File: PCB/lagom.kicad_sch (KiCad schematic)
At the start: 154 parts

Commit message: Matrix almost done
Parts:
- added D? (x2): D_Small, Keebio-Parts:Diode, symbol Device:D_Small
- added SW?: KEYSW, Button_Switch_Keyboard:SW_Cherry_MX_7u_PCB, symbol keyboard_parts:KEYSW
- added SW? (x2): KEYSW, Button_Switch_Keyboard:SW_Cherry_MX_1.00u_PCB, symbol keyboard_parts:KEYSW
- added SW?: KEYSW, Button_Switch_Keyboard:SW_Cherry_MX_1.50u_PCB, symbol keyboard_parts:KEYSW
- added SW? (x2): KEYSW, Button_Switch_Keyboard:SW_Cherry_MX_1.25u_PCB, symbol keyboard_parts:KEYSW
- SW?: footprint Button_Switch_Keyboard:SW_Cherry_MX_1.25u_PCB -> Button_Switch_Keyboard:SW_Cherry_MX_1.50u_PCB
- SW? (x2): footprint Button_Switch_Keyboard:SW_Cherry_MX_1.00u_PCB -> Button_Switch_Keyboard:SW_Cherry_MX_1.25u_PCB
- SW?: footprint Button_Switch_Keyboard:SW_Cherry_MX_1.00u_PCB -> Button_Switch_Keyboard:SW_Cherry_MX_1.50u_PCB
- SW?: footprint Button_Switch_Keyboard:SW_Cherry_MX_1.25u_PCB -> Button_Switch_Keyboard:SW_Cherry_MX_1.00u_PCB
- SW?: footprint Button_Switch_Keyboard:SW_Cherry_MX_1.25u_PCB -> Button_Switch_Keyboard:SW_Cherry_MX_ISOEnter_PCB
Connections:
- net RotA: now also D?.2 (A); no longer D?.2 (A)
- net RotB: now also SW?.1, SW?.1, SW?.1, SW?.1; no longer SW?.1, SW?.1, SW?.1, SW?.1
- net RotC: now also D?.2 (A); no longer D?.2 (A)
- net RotD: now also SW?.1, SW?.1, SW?.1, SW?.1, SW?.1; no longer SW?.1, SW?.1, SW?.1, SW?.1
- net rowG: now also D?.1 (K), D?.1 (K); no longer U?.20 (A3/PF4)
- net at SW?.1, SW?.1, SW?.1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: now also SW?.1 (x2)
- net at SW?.1, SW?.1, SW?.1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: now also SW?.1
- net at D?.2 (A), SW?.2: now also SW?.2 (x3)
- net at SW?.1, SW?.1, SW?.1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: now also SW?.1
- net at D?.2 (A), SW?.2, SW?.2: now also SW?.2
- new net: SW?.1, SW?.1, SW?.1, SW?.1, SW?.1 (x2)
- new net: D?.2 (A), SW?.2 (x2)
- new net rowH: U?.20 (A3/PF4)
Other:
- moved on the sheet: SW?

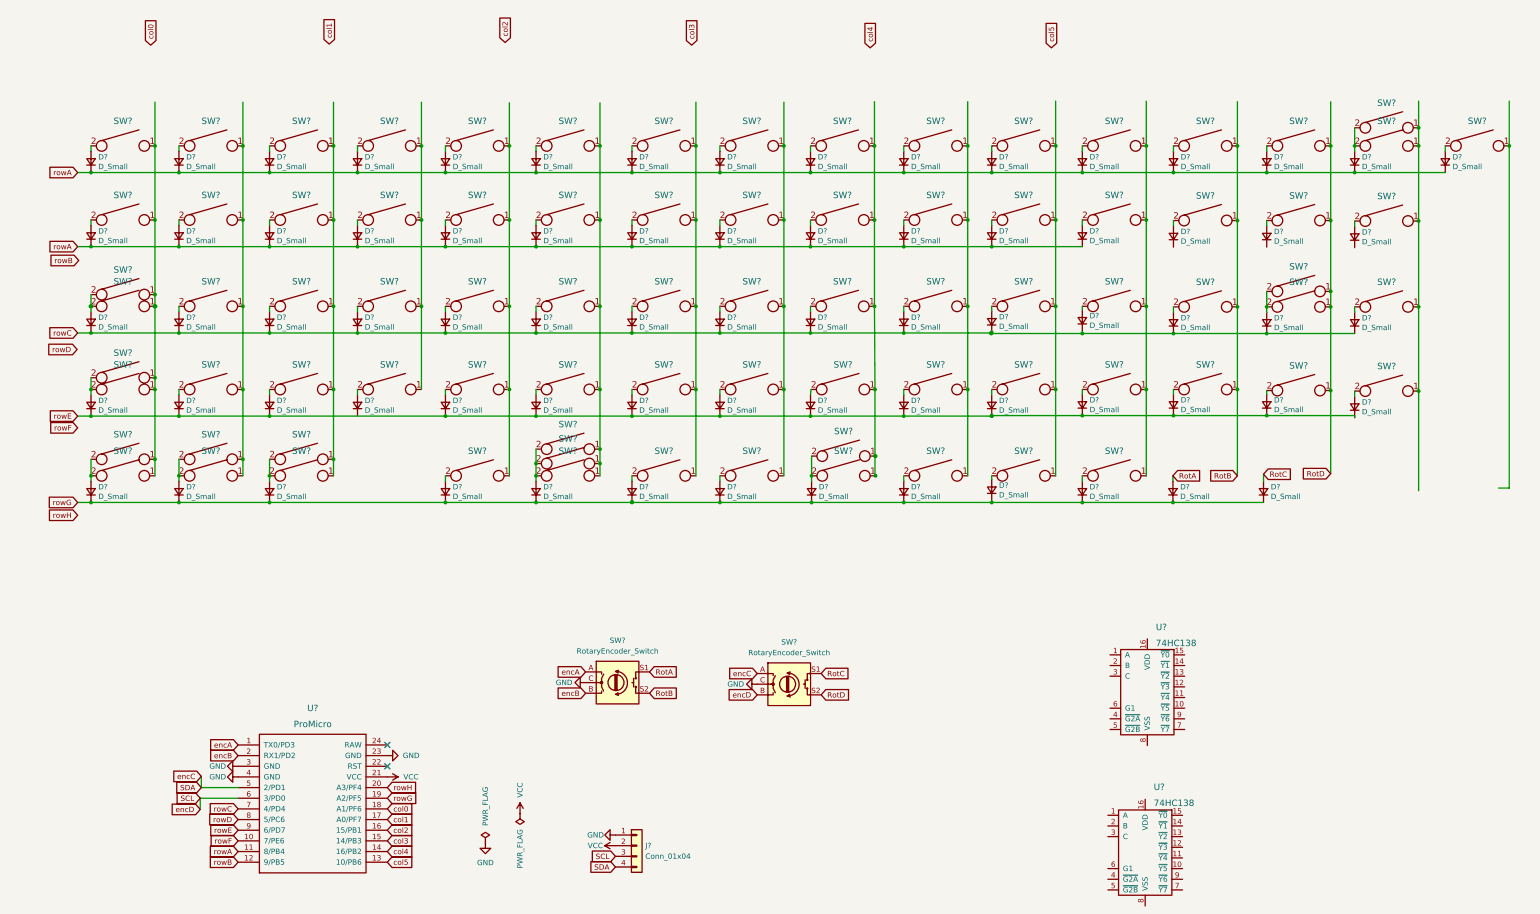
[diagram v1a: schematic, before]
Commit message: Matrix complete, wiring schematic
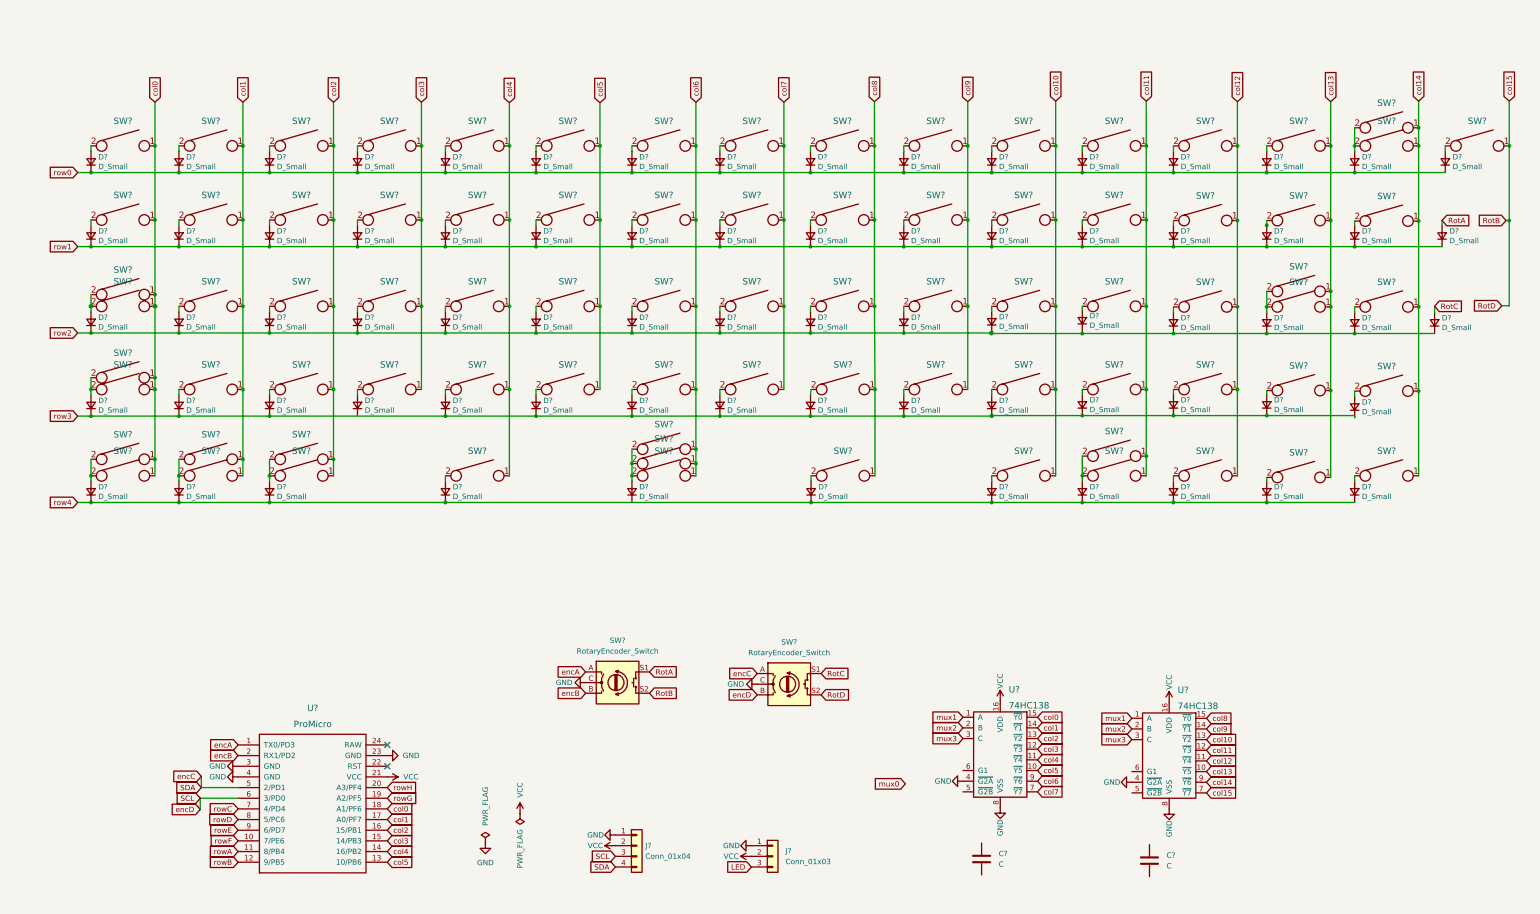
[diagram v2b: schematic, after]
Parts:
- added C? (x2): C, symbol Device:C
- added J?: Conn_01x03, symbol Connector_Generic:Conn_01x03
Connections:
- net GND: now also U?.4 (~{G2A}), U?.4 (~{G2A}), U?.8 (VSS), U?.8 (VSS), J?.1 (Pin_1)
- net RotB: now also SW?.1, SW?.S2, U?.7 (~{Y7}); no longer SW?.1, SW?.1, SW?.1, SW?.1
- net VCC: now also U?.16 (VDD), U?.16 (VDD), J?.2 (Pin_2)
- net col0: now also SW?.1, SW?.1, SW?.1, SW?.1, SW?.1, SW?.1, SW?.1, SW?.1, U?.15 (~{Y0})
- net col1: now also SW?.1, SW?.1, SW?.1, SW?.1, SW?.1, SW?.1, U?.14 (~{Y1})
- net col2: now also SW?.1, SW?.1, SW?.1, SW?.1, SW?.1, SW?.1, U?.13 (~{Y2})
- net col3: now also SW?.1, SW?.1, SW?.1, SW?.1, U?.12 (~{Y3})
- net col4: now also SW?.1, SW?.1, SW?.1, SW?.1, SW?.1, U?.11 (~{Y4})
- net col5: now also SW?.1, SW?.1, SW?.1, SW?.1, U?.10 (~{Y5})
- net rowA: no longer D?.1 (K), D?.1 (K), D?.1 (K), D?.1 (K), D?.1 (K), D?.1 (K), D?.1 (K), D?.1 (K), D?.1 (K), D?.1 (K), D?.1 (K), D?.1 (K), D?.1 (K), D?.1 (K), D?.1 (K), D?.1 (K), D?.1 (K), D?.1 (K), D?.1 (K), D?.1 (K), D?.1 (K), D?.1 (K), D?.1 (K), D?.1 (K)
- net rowC: no longer D?.1 (K), D?.1 (K), D?.1 (K), D?.1 (K), D?.1 (K), D?.1 (K), D?.1 (K), D?.1 (K), D?.1 (K), D?.1 (K), D?.1 (K), D?.1 (K), D?.1 (K), D?.1 (K), D?.1 (K)
- net rowE: no longer D?.1 (K), D?.1 (K), D?.1 (K), D?.1 (K), D?.1 (K), D?.1 (K), D?.1 (K), D?.1 (K), D?.1 (K), D?.1 (K), D?.1 (K), D?.1 (K), D?.1 (K), D?.1 (K)
- net rowG: no longer D?.1 (K), D?.1 (K), D?.1 (K), D?.1 (K), D?.1 (K), D?.1 (K), D?.1 (K), D?.1 (K), D?.1 (K), D?.1 (K), D?.1 (K), D?.1 (K), D?.1 (K)
- net col8: now reaches SW?.1, SW?.1, SW?.1, SW?.1
- net col8: now also SW?.1, U?.15 (~{Y0}); no longer SW?.1, SW?.1
- net col10: now reaches SW?.1, SW?.1, SW?.1, SW?.1
- net col10: now also SW?.1, U?.13 (~{Y2}); no longer SW?.1
- net col9: now reaches SW?.1, SW?.1, SW?.1, SW?.1
- net col9: now also U?.14 (~{Y1}); no longer SW?.1
- net col14: now reaches SW?.1, SW?.1, SW?.1, SW?.1, SW?.1
- net col14: now also SW?.1, U?.9 (~{Y6})
- net row1: now reaches D?.1 (K)
- net row1: now also D?.1 (K), D?.1 (K), D?.1 (K), D?.1 (K), D?.1 (K), D?.1 (K), D?.1 (K), D?.1 (K), D?.1 (K), D?.1 (K), D?.1 (K), D?.1 (K), D?.1 (K), D?.1 (K), D?.1 (K)
- net col7: now reaches SW?.1, SW?.1, SW?.1, SW?.1
- net col7: now also U?.7 (~{Y7}); no longer SW?.1
- net col6: now reaches SW?.1, SW?.1, SW?.1, SW?.1
- net col6: now also SW?.1, SW?.1, SW?.1, U?.9 (~{Y6}); no longer SW?.1
- net col11: now reaches SW?.1, SW?.1, SW?.1, SW?.1
- net col11: now also SW?.1, SW?.1, U?.12 (~{Y3}); no longer SW?.1
- net mux1: now reaches U?.1 (A)
- net mux1: now also U?.1 (A)
- net mux2: now reaches U?.2 (B)
- net mux2: now also U?.2 (B)
- net mux3: now reaches U?.3 (C)
- net mux3: now also U?.3 (C)
- net col13: now reaches U?.10 (~{Y5})
- net col13: now also SW?.1, SW?.1, SW?.1, SW?.1, SW?.1, SW?.1
- net col12: now reaches U?.11 (~{Y4})
- net col12: now also SW?.1, SW?.1, SW?.1, SW?.1, SW?.1
- removed net RotD: SW?.1, SW?.1, SW?.1, SW?.1, SW?.1, SW?.S2
- new net LED: J?.3 (Pin_3)
- new net row0: D?.1 (K), D?.1 (K), D?.1 (K), D?.1 (K), D?.1 (K), D?.1 (K), D?.1 (K), D?.1 (K), D?.1 (K), D?.1 (K), D?.1 (K), D?.1 (K)
- new net row2: D?.1 (K), D?.1 (K), D?.1 (K), D?.1 (K), D?.1 (K), D?.1 (K), D?.1 (K), D?.1 (K), D?.1 (K), D?.1 (K), D?.1 (K), D?.1 (K), D?.1 (K), D?.1 (K), D?.1 (K), D?.1 (K)
- new net row3: D?.1 (K), D?.1 (K), D?.1 (K), D?.1 (K), D?.1 (K), D?.1 (K), D?.1 (K), D?.1 (K), D?.1 (K), D?.1 (K), D?.1 (K), D?.1 (K), D?.1 (K), D?.1 (K)
- new net row4: D?.1 (K), D?.1 (K), D?.1 (K), D?.1 (K), D?.1 (K), D?.1 (K), D?.1 (K), D?.1 (K), D?.1 (K), D?.1 (K)
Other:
- moved on the sheet: D?, SW?, U?

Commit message: Schematic complete
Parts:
- C1, C2: renamed from C?; value C -> 0.1uF
- D1: renamed from D?; footprint Keebio-Parts:Diode -> Diode_THT:D_DO-35_SOD27_P7.62mm_Horizontal
- gave numbers to parts that had none: 162
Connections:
- net rowA is gone; now on net row3: U1.11 (8/PB4)
- net rowB is gone; now on net row4: U1.12 (9/PB5)
- net rowC is gone; now on net LED: U1.7 (4/PD4)
- net rowD is gone; now on net row0: U1.8 (5/PC6)
- net rowE is gone; now on net row1: U1.9 (6/PD7)
- net rowF is gone; now on net row2: U1.10 (7/PE6)
- net rowG is gone; now on net encB: U1.19 (A2/PF5)
- net rowH is gone; now on net encA: U1.20 (A3/PF4)
- net GND: now also C1.2, C2.2, U3.5 (~{G2B})
- net SCL: no longer SW84.B
- net SDA: no longer SW84.A
- net VCC: now also C1.1, C2.1, U2.6 (G1)
- net col0: no longer U1.18 (A1/PF6)
- net col1: no longer U1.17 (A0/PF7)
- net col2: no longer U1.16 (15/PB1)
- net col3: no longer U1.15 (14/PB3)
- net col4: no longer U1.14 (16/PB2)
- net col5: no longer U1.13 (10/PB6)
- net encA: no longer U1.1 (TX0/PD3)
- net encB: no longer U1.2 (RX1/PD2)
- net mux0: now also U1.16 (15/PB1), U2.5 (~{G2B}), U3.6 (G1)
- net mux1: now also U1.15 (14/PB3)
- net mux2: now also U1.14 (16/PB2)
- net mux3: now also U1.13 (10/PB6)
- net row3: now also D55.1 (K)
- net row4: now also D68.1 (K)
- new net encC: SW84.A, U1.18 (A1/PF6)
- new net encD: SW84.B, U1.17 (A0/PF7)
- no-connect marks 2 -> 4
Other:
- moved on the sheet: C1, C2, U1, U3

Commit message: PCB layout done
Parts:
- C1, C2: footprint (none) -> Capacitor_THT:C_Disc_D4.7mm_W2.5mm_P5.00mm
- J2: footprint (none) -> Connector_PinSocket_2.54mm:PinSocket_1x03_P2.54mm_Vertical
- SW13, SW17, SW29: footprint Button_Switch_Keyboard:SW_Cherry_MX_1.50u_PCB -> Button_Switch_Keyboard:SW_Cherry_MX_1.00u_PCB
- U2, U3: footprint (none) -> Package_DIP:DIP-16_W7.62mm_Socket
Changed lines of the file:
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@@
       (effects (font (size 1.27 1.27)) (justify left))
     )
-    (property "Footprint" "" (id 2) (at 246.8372 199.898 0)
+    (property "Footprint" "Capacitor_THT:C_Disc_D4.7mm_W2.5mm_P5.00mm" (id 2) (at 246.8372 199.898 0)
       (effects (font (size 1.27 1.27)) hide)
     )
@@
   (symbol (lib_id "w_logic:74HC138") (at 269.621 195.58 0) (unit 1)
     (in_bom yes) (on_board yes) (fields_autoplaced)
-    (property "Reference" "U2" (id 0) (at 271.6404 180.086 0)
+    (property "Reference" "U2" (id 0) (at 271.6404 180.34 0)
       (effects (font (size 1.524 1.524)) (justify left))
     )
-    (property "Value" "74HC138" (id 1) (at 271.6404 183.896 0)
+    (property "Value" "74HC138" (id 1) (at 271.6404 184.15 0)
       (effects (font (size 1.524 1.524)) (justify left))
     )
-    (property "Footprint" "" (id 2) (at 269.621 195.58 0)
-      (effects (font (size 1.524 1.524)))
+    (property "Footprint" "Package_DIP:DIP-16_W7.62mm_Socket" (id 2) (at 269.621 195.58 0)
+      (effects (font (size 1.524 1.524)) hide)
     )
     (property "Datasheet" "/mnt/dati/documenti/Elettronica/DATA_SHEET/Elettronici/Integrati/Digitali/Registri/NXP_74HC138_74HCT138.pdf" (id 3) (at 271.6404 183.896 0)
@@
       (effects (font (size 1.524 1.524)) hide)
     )
-    (property "Footprint" "Button_Switch_Keyboard:SW_Cherry_MX_1.50u_PCB" (id 2) (at 383.286 50.546 0)
+    (property "Footprint" "Button_Switch_Keyboard:SW_Cherry_MX_1.00u_PCB" (id 2) (at 383.286 50.546 0)
       (effects (font (size 1.524 1.524)) hide)
     )
@@
       (effects (font (size 1.524 1.524)) hide)
     )
-    (property "Footprint" "Button_Switch_Keyboard:SW_Cherry_MX_1.50u_PCB" (id 2) (at 296.799 50.546 0)
+    (property "Footprint" "Button_Switch_Keyboard:SW_Cherry_MX_1.00u_PCB" (id 2) (at 296.799 50.546 0)
       (effects (font (size 1.524 1.524)) hide)
     )
@@
       (effects (font (size 1.27 1.27)) (justify left))
     )
-    (property "Footprint" "" (id 2) (at 215.392 219.837 0)
+    (property "Footprint" "Connector_PinSocket_2.54mm:PinSocket_1x03_P2.54mm_Vertical" (id 2) (at 215.392 219.837 0)
       (effects (font (size 1.27 1.27)) hide)
     )
@@
       (effects (font (size 1.27 1.27)) (justify left))
     )
-    (property "Footprint" "" (id 2) (at 305.5112 198.882 0)
+    (property "Footprint" "Capacitor_THT:C_Disc_D4.7mm_W2.5mm_P5.00mm" (id 2) (at 305.5112 198.882 0)
       (effects (font (size 1.27 1.27)) hide)
     )
@@
   (symbol (lib_id "w_logic:74HC138") (at 328.93 195.199 0) (unit 1)
     (in_bom yes) (on_board yes) (fields_autoplaced)
-    (property "Reference" "U3" (id 0) (at 330.9494 179.578 0)
+    (property "Reference" "U3" (id 0) (at 330.9494 179.07 0)
       (effects (font (size 1.524 1.524)) (justify left))
     )
-    (property "Value" "74HC138" (id 1) (at 330.9494 183.388 0)
+    (property "Value" "74HC138" (id 1) (at 330.9494 182.88 0)
       (effects (font (size 1.524 1.524)) (justify left))
     )
-    (property "Footprint" "" (id 2) (at 328.93 195.199 0)
-      (effects (font (size 1.524 1.524)))
+    (property "Footprint" "Package_DIP:DIP-16_W7.62mm_Socket" (id 2) (at 328.93 195.199 0)
+      (effects (font (size 1.524 1.524)) hide)
     )
     (property "Datasheet" "/mnt/dati/documenti/Elettronica/DATA_SHEET/Elettronici/Integrati/Digitali/Registri/NXP_74HC138_74HCT138.pdf" (id 3) (at 330.9494 183.515 0)
@@
       (effects (font (size 1.524 1.524)) hide)
     )
-    (property "Footprint" "Button_Switch_Keyboard:SW_Cherry_MX_1.50u_PCB" (id 2) (at 296.799 68.199 0)
+    (property "Footprint" "Button_Switch_Keyboard:SW_Cherry_MX_1.00u_PCB" (id 2) (at 296.799 68.199 0)
       (effects (font (size 1.524 1.524)) hide)
     )
@@
     )
     (path "/bc00cb6d-ff28-45b9-b930-be73b03fd96d"
-      (reference "C1") (unit 1) (value "0.1uF") (footprint "")
+      (reference "C1") (unit 1) (value "0.1uF") (footprint "Capacitor_THT:C_Disc_D4.7mm_W2.5mm_P5.00mm")
     )
     (path "/0fd8c6ab-3384-49aa-8e48-3f4df84bc20e"
-      (reference "C2") (unit 1) (value "0.1uF") (footprint "")
+      (reference "C2") (unit 1) (value "0.1uF") (footprint "Capacitor_THT:C_Disc_D4.7mm_W2.5mm_P5.00mm")
     )
     (path "/afa695ae-8ccf-42d3-9dcb-5e731da4e36c"
@@
     )
     (path "/afffe1fe-d14c-481c-bd58-ae7a8ca3d519"
-      (reference "J2") (unit 1) (value "Conn_01x03") (footprint "")
+      (reference "J2") (unit 1) (value "Conn_01x03") (footprint "Connector_PinSocket_2.54mm:PinSocket_1x03_P2.54mm_Vertical")
     )
     (path "/a5c5762f-a0e0-401e-8bc4-621198606bcb"
@@
     )
     (path "/9c21fdb3-4254-429a-8fa6-c29cf995b177"
-      (reference "SW13") (unit 1) (value "KEYSW") (footprint "Button_Switch_Keyboard:SW_Cherry_MX_1.50u_PCB")
+      (reference "SW13") (unit 1) (value "KEYSW") (footprint "Button_Switch_Keyboard:SW_Cherry_MX_1.00u_PCB")
     )
     (path "/fec9eaae-d6bc-4df4-9d8e-a08e2c64f06c"
@@
     )
     (path "/9808b20e-3499-4769-b8e9-46d57a37bd43"
-      (reference "SW17") (unit 1) (value "KEYSW") (footprint "Button_Switch_Keyboard:SW_Cherry_MX_1.50u_PCB")
+      (reference "SW17") (unit 1) (value "KEYSW") (footprint "Button_Switch_Keyboard:SW_Cherry_MX_1.00u_PCB")
     )
     (path "/05d4fb02-3c60-405c-9080-fb8446959d7e"
@@
     )
     (path "/e9fcf385-9380-4c87-8aca-dfe9bbcc7460"
-      (reference "SW29") (unit 1) (value "KEYSW") (footprint "Button_Switch_Keyboard:SW_Cherry_MX_1.50u_PCB")
+      (reference "SW29") (unit 1) (value "KEYSW") (footprint "Button_Switch_Keyboard:SW_Cherry_MX_1.00u_PCB")
     )
     (path "/71d08102-98f4-4a2d-8663-96fe9600f004"
@@
     )
     (path "/6894fe82-0ee5-4f27-a435-6dbd0d79b968"
-      (reference "U2") (unit 1) (value "74HC138") (footprint "")
+      (reference "U2") (unit 1) (value "74HC138") (footprint "Package_DIP:DIP-16_W7.62mm_Socket")
     )
     (path "/c92f95b2-2642-46df-8ce4-131bc603da4f"
-      (reference "U3") (unit 1) (value "74HC138") (footprint "")
+      (reference "U3") (unit 1) (value "74HC138") (footprint "Package_DIP:DIP-16_W7.62mm_Socket")
     )
   )

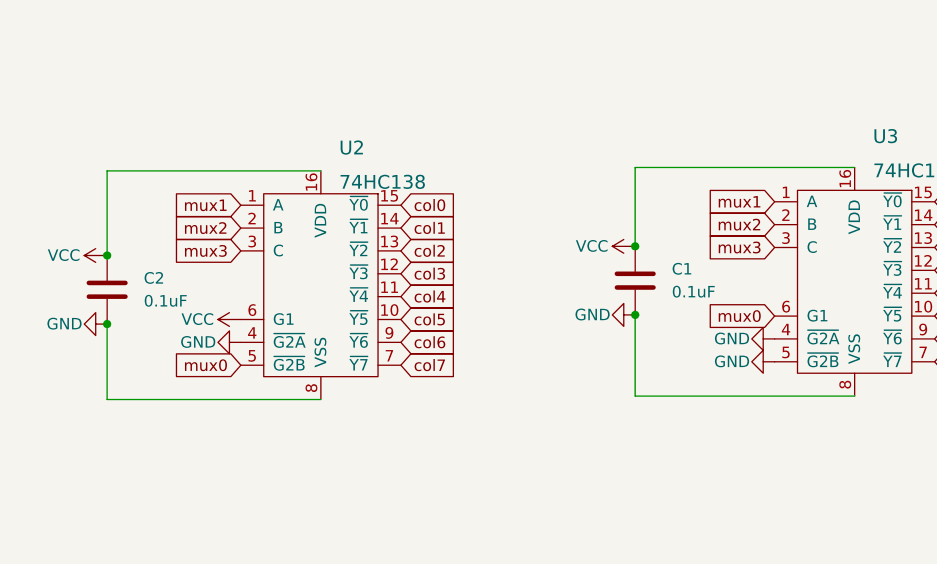
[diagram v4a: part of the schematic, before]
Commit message: demux pin change
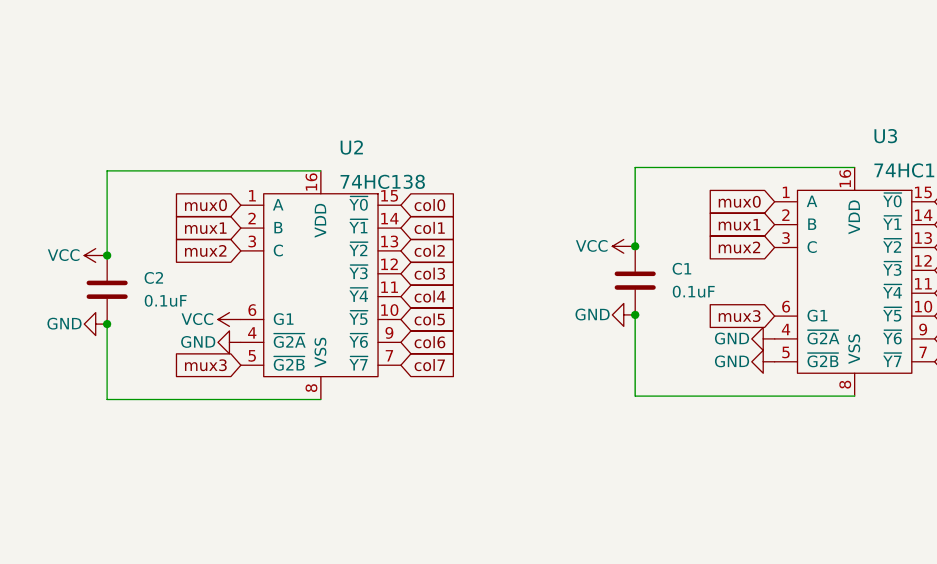
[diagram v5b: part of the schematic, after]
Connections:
- net mux0: now also U2.1 (A), U3.1 (A); no longer U2.5 (~{G2B}), U3.6 (G1)
- net mux1: now also U2.2 (B), U3.2 (B); no longer U2.1 (A), U3.1 (A)
- net mux2: now also U2.3 (C), U3.3 (C); no longer U2.2 (B), U3.2 (B)
- net mux3: now also U2.5 (~{G2B}), U3.6 (G1); no longer U2.3 (C), U3.3 (C)

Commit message: Layout and diode placement basically done
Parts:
- D10, D11, D12, D13, D14, D15, D16, D17, D18, D19, D2, D20, D21, D22, D23, D24, D25, D26, D27, D28, D29, D3, D30, D31, D32, D33, D34, D35, D36, D37, D38, D39, D4, D40, D41, D42, D43, D44, D45, D46, D47, D48, D49, D5, D50, D51, D52, D53, D54, D55, D56, D57, D58, D59, D6, D60, D61, D62, D63, D64, D65, D66, D67, D68, D69, D7, D70, D71, D72, D73, D74, D8, D9: footprint Keebio-Parts:Diode -> Diode_THT:D_DO-34_SOD68_P7.62mm_Horizontal
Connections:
- net row0: now also D13.1 (K), D14.1 (K), D15.1 (K), D16.1 (K)

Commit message: PCB mostly done
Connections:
- net encA: now also U1.18 (A1/PF6); no longer U1.20 (A3/PF4)
- net encB: now also U1.17 (A0/PF7); no longer U1.19 (A2/PF5)
- net encC: now also U1.20 (A3/PF4); no longer U1.18 (A1/PF6)
- net encD: now also U1.19 (A2/PF5); no longer U1.17 (A0/PF7)
- net row0: now also U1.12 (9/PB5); no longer U1.8 (5/PC6)
- net row1: now also U1.11 (8/PB4); no longer U1.9 (6/PD7)
- net row3: now also U1.9 (6/PD7); no longer U1.11 (8/PB4)
- net row4: now also U1.8 (5/PC6); no longer U1.12 (9/PB5)
